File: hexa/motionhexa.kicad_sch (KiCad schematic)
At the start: 1 part, among them J1 Conn_01x04_Socket

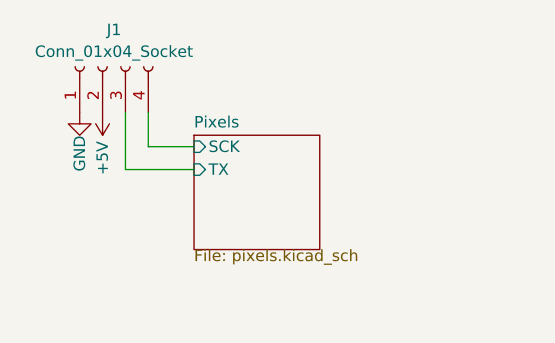
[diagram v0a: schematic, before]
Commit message: add photosensor back in, but on the front of the hexa
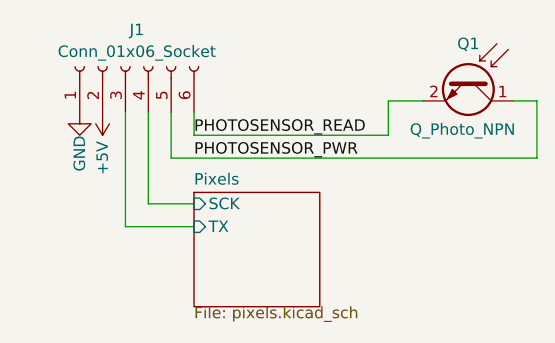
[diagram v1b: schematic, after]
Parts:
- added Q1: Q_Photo_NPN, Resistor_SMD:R_0603_1608Metric, symbol Device:Q_Photo_NPN
- J1: value Conn_01x04_Socket -> Conn_01x06_Socket; symbol Connector:Conn_01x04_Socket -> Connector:Conn_01x06_Socket; now in the parts list
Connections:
- new net PHOTOSENSOR_PWR: J1.5 (Pin_5), Q1.1 (C)
- new net PHOTOSENSOR_READ: J1.6 (Pin_6), Q1.2 (E)
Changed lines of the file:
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@@
 	(wire
 		(pts
-			(xy 97.79 60.96) (xy 105.41 60.96)
-		)
-		(stroke
-			(width 0)
-			(type default)
-		)
-	)
-	(wire
-		(pts
-			(xy 100.33 58.42) (xy 100.33 54.61)
-		)
-		(stroke
-			(width 0)
-			(type default)
-		)
-	)
-	(wire
-		(pts
-			(xy 105.41 58.42) (xy 100.33 58.42)
-		)
-		(stroke
-			(width 0)
-			(type default)
-		)
-	)
-	(wire
-		(pts
-			(xy 97.79 54.61) (xy 97.79 60.96)
-		)
-		(stroke
-			(width 0)
-			(type default)
+			(xy 97.79 67.31) (xy 105.41 67.31)
+		)
+		(stroke
+			(width 0)
+			(type default)
+		)
+	)
+	(wire
+		(pts
+			(xy 102.87 59.69) (xy 143.51 59.69)
+		)
+		(stroke
+			(width 0)
+			(type default)
+		)
+	)
+	(wire
+		(pts
+			(xy 102.87 54.61) (xy 102.87 59.69)
+		)
+		(stroke
+			(width 0)
+			(type default)
+		)
+	)
+	(wire
+		(pts
+			(xy 130.81 53.34) (xy 127 53.34)
+		)
+		(stroke
+			(width 0)
+			(type default)
+		)
+	)
+	(wire
+		(pts
+			(xy 143.51 53.34) (xy 140.97 53.34)
+		)
+		(stroke
+			(width 0)
+			(type default)
+		)
+	)
+	(wire
+		(pts
+			(xy 105.41 57.15) (xy 127 57.15)
+		)
+		(stroke
+			(width 0)
+			(type default)
+		)
+	)
+	(wire
+		(pts
+			(xy 105.41 54.61) (xy 105.41 57.15)
+		)
+		(stroke
+			(width 0)
+			(type default)
+		)
+	)
+	(wire
+		(pts
+			(xy 100.33 64.77) (xy 100.33 54.61)
+		)
+		(stroke
+			(width 0)
+			(type default)
+		)
+	)
+	(wire
+		(pts
+			(xy 143.51 53.34) (xy 143.51 59.69)
+		)
+		(stroke
+			(width 0)
+			(type default)
+		)
+	)
+	(wire
+		(pts
+			(xy 105.41 64.77) (xy 100.33 64.77)
+		)
+		(stroke
+			(width 0)
+			(type default)
+		)
+	)
+	(wire
+		(pts
+			(xy 127 53.34) (xy 127 57.15)
+		)
+		(stroke
+			(width 0)
+			(type default)
+		)
+	)
+	(wire
+		(pts
+			(xy 97.79 54.61) (xy 97.79 67.31)
+		)
+		(stroke
+			(width 0)
+			(type default)
+		)
+	)
+	(label "PHOTOSENSOR_PWR"
+		(at 105.41 59.69 0)
+		(fields_autoplaced yes)
+		(effects
+			(font
+				(size 1.27 1.27)
+			)
+			(justify left bottom)
+		)
+	)
+	(label "PHOTOSENSOR_READ"
+		(at 105.41 57.15 0)
+		(fields_autoplaced yes)
+		(effects
+			(font
+				(size 1.27 1.27)
+			)
+			(justify left bottom)
 		)
 	)
@@
 	)
 	(symbol
-		(lib_id "Connector:Conn_01x04_Socket")
-		(at 95.25 49.53 90)
+		(lib_id "Connector:Conn_01x06_Socket")
+		(at 97.79 49.53 90)
 		(unit 1)
 		(exclude_from_sim no)
-		(in_bom no)
+		(in_bom yes)
 		(on_board yes)
 		(dnp no)
 		(fields_autoplaced yes)
 		(property "Reference" "J1"
-			(at 96.52 45.4363 90)
-			(effects
-				(font
-					(size 1.27 1.27)
-				)
-			)
-		)
-		(property "Value" "Conn_01x04_Socket"
-			(at 96.52 47.8606 90)
+			(at 99.06 45.4363 90)
+			(effects
+				(font
+					(size 1.27 1.27)
+				)
+			)
+		)
+		(property "Value" "Conn_01x06_Socket"
+			(at 99.06 47.8606 90)
 			(effects
 				(font
@@
 		)
 		(property "Footprint" "motionhexa:hexacontroller_pads"
-			(at 95.25 49.53 0)
+			(at 97.79 49.53 0)
 			(effects
 				(font
@@
 		)
 		(property "Datasheet" "~"
-			(at 95.25 49.53 0)
-			(effects
-				(font
-					(size 1.27 1.27)
-				)
-				(hide yes)
-			)
-		)
-		(property "Description" "Generic connector, single row, 01x04, script generated"
-			(at 95.25 49.53 0)
+			(at 97.79 49.53 0)
+			(effects
+				(font
+					(size 1.27 1.27)
+				)
+				(hide yes)
+			)
+		)
+		(property "Description" "Generic connector, single row, 01x06, script generated"
+			(at 97.79 49.53 0)
 			(effects
 				(font
@@
 		)
 		(property "Designation" ""
-			(at 95.25 49.53 0)
+			(at 97.79 49.53 0)
 			(effects
 				(font
@@
 		)
 		(pin "1"
+		)
+		(pin "5"
+		)
+		(pin "6"
 		)
 		(instances
@@
 		)
 	)
+	(symbol
+		(lib_id "Device:Q_Photo_NPN")
+		(at 135.89 50.8 270)
+		(unit 1)
+		(exclude_from_sim no)
+		(in_bom yes)
+		(on_board yes)
+		(dnp no)
+		(property "Reference" "Q1"
+			(at 135.89 46.99 90)
+			(effects
+				(font
+					(size 1.27 1.27)
+				)
+			)
+		)
+		(property "Value" "Q_Photo_NPN"
+			(at 135.255 56.515 90)
+			(effects
+				(font
+					(size 1.27 1.27)
+				)
+			)
+		)
+		(property "Footprint" "Resistor_SMD:R_0603_1608Metric"
+			(at 138.43 55.88 0)
+			(effects
+				(font
+					(size 1.27 1.27)
+				)
+				(hide yes)
+			)
+		)
+		(property "Datasheet" "~"
+			(at 135.89 50.8 0)
+			(effects
+				(font
+					(size 1.27 1.27)
+				)
+				(hide yes)
+			)
+		)
+		(property "Description" ""
+			(at 135.89 50.8 0)
+			(effects
+				(font
+					(size 1.27 1.27)
+				)
+				(hide yes)
+			)
+		)
+		(property "Designation" "ALS-PT19-315C/L177/TR8"
+			(at 135.89 50.8 0)
+			(effects
+				(font
+					(size 1.27 1.27)
+				)
+				(hide yes)
+			)
+		)
+		(property "LCSC" "C146233"
+			(at 135.89 50.8 90)
+			(effects
+				(font
+					(size 1.27 1.27)
+				)
+				(hide yes)
+			)
+		)
+		(pin "2"
+		)
+		(pin "1"
+		)
+		(instances
+			(project "motionhexa"
+				(path "/532d7ce0-7387-4a95-852a-321dca6ae013"
+					(reference "Q1")
+					(unit 1)
+				)
+			)
+		)
+	)
 	(sheet
-		(at 105.41 57.15)
+		(at 105.41 63.5)
 		(size 13.97 12.7)
 		(fields_autoplaced yes)
@@
 		)
 		(property "Sheetname" "Pixels"
-			(at 105.41 56.4384 0)
+			(at 105.41 62.7884 0)
 			(effects
 				(font
@@
 		)
 		(property "Sheetfile" "pixels.kicad_sch"
-			(at 105.41 69.7996 0)
+			(at 105.41 76.1496 0)
 			(effects
 				(font
@@
 		)
 		(pin "SCK" input
-			(at 105.41 58.42 180)
+			(at 105.41 64.77 180)
 			(effects
 				(font
@@
 		)
 		(pin "TX" input
-			(at 105.41 60.96 180)
-			(effects
-				(font
+			(at 105.41 67.31 180)
+			(effects
+				(font

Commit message: remove connector from bom, positions
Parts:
- J1: now left out of the parts list
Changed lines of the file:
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@@
 		(unit 1)
 		(exclude_from_sim no)
-		(in_bom yes)
+		(in_bom no)
 		(on_board yes)
 		(dnp no)
